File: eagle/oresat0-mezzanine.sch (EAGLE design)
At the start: 29 parts, among them J1 R107064070, J10 R107064070, J2 R107064070, J3 R107064070, J4 R107064070, J5 R107064070, J6 R107064070, J7 R107064070, J8 R107064070, J9 R107064070, U1 QBA-07+, U2 QBA-07+, U3 QBA-07+, U7 QCN-27+, U8 QCN-27+, U9 QCN-27+

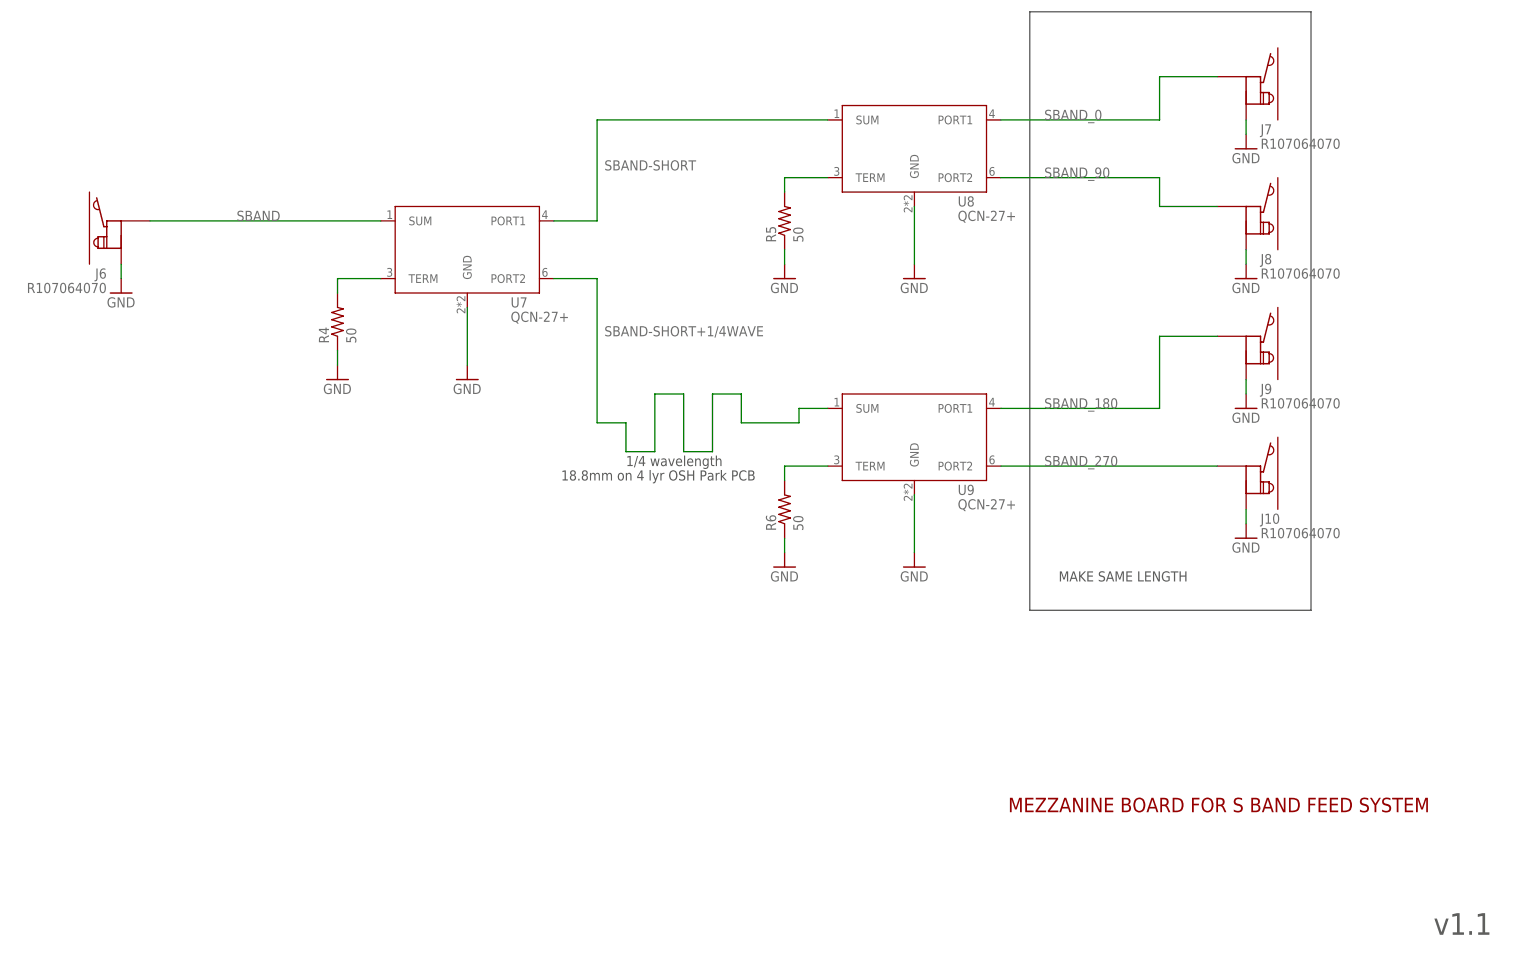
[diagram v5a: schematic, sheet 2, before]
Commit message: replaced S-band net labels with L1-band labels, swapped the S-band hybrids with L-band hybrids, recalculated 1/4 wavelength trace length, routed a new short+1/4 wavelength trace
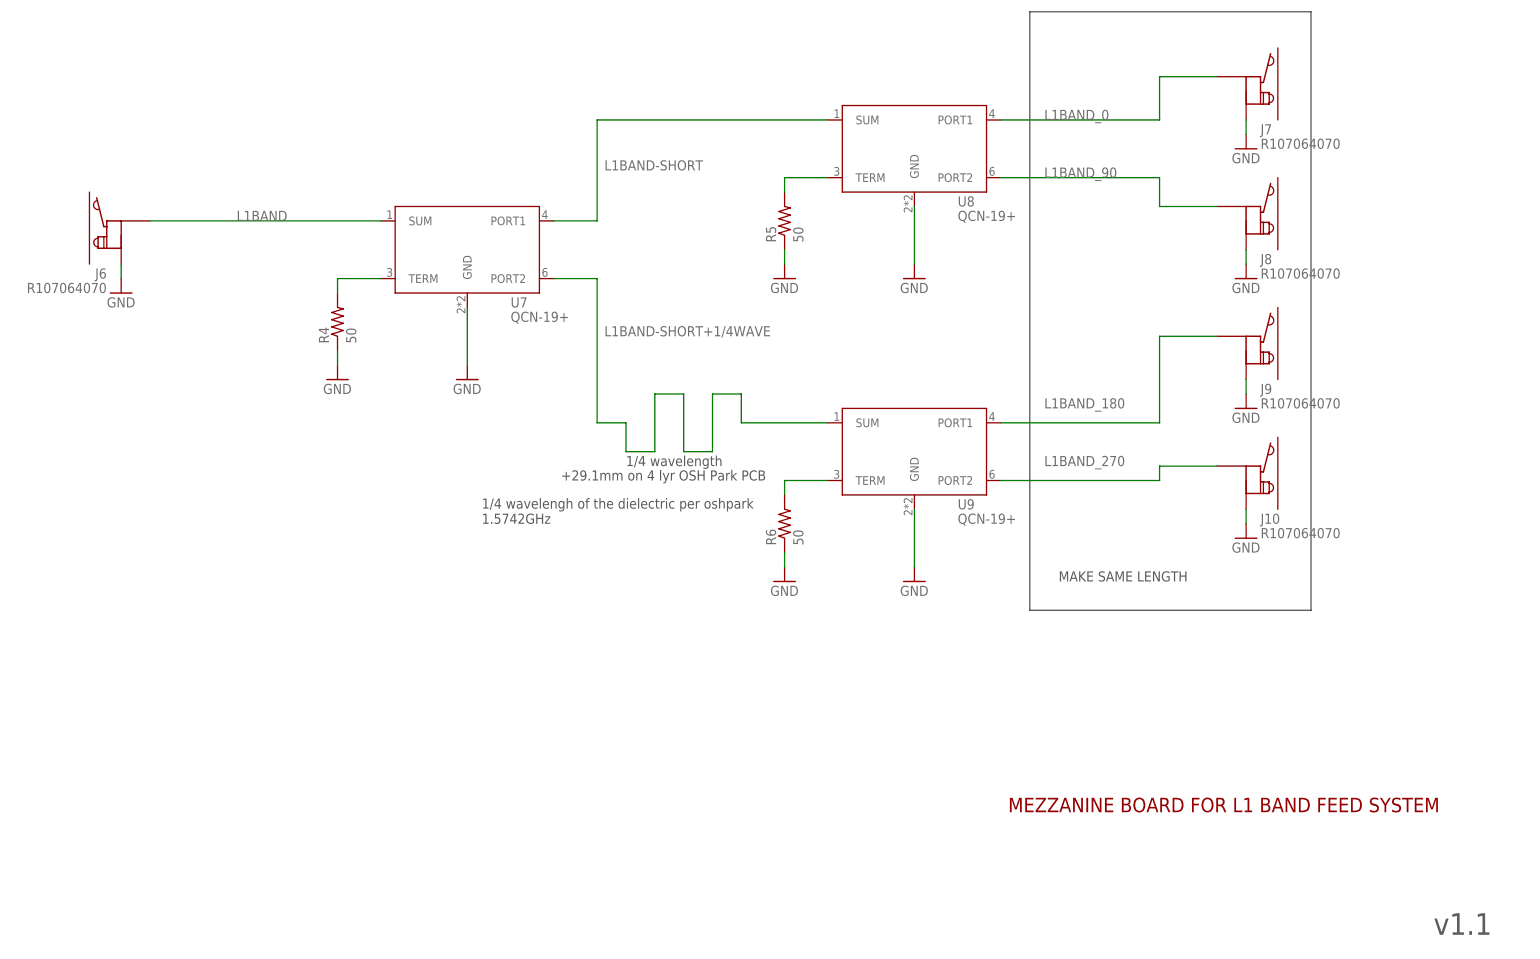
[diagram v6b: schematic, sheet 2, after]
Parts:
- U7, U8, U9: value QCN-27+ -> QCN-19+
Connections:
- net SBAND renamed L1BAND
- net SBAND-SHORT renamed L1BAND-SHORT
- net SBAND-SHORT+1/4WAVE renamed L1BAND-SHORT+1/4WAVE
- net SBAND_0 renamed L1BAND_0
- net SBAND_180 renamed L1BAND_180
- net SBAND_270 renamed L1BAND_270
- net SBAND_90 renamed L1BAND_90
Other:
- note added: "+29.1mm on 4 lyr OSH Park PCB"
- note added: "1/4 wavelengh of the dielectric per oshpark 1.5742GHz"
- note added: "MEZZANINE BOARD FOR L1 BAND FEED SYSTEM"
- note removed: "18.8mm on 4 lyr OSH Park PCB"
- note removed: "MEZZANINE BOARD FOR S BAND FEED SYSTEM"
- moved on the sheet: R6, U9
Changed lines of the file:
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@@
 <setting verticaltext="up"/>
 </settings>
-<grid distance="0.1" unitdist="inch" unit="inch" style="lines" multiple="1" display="no" altdistance="0.01" altunitdist="inch" altunit="inch"/>
+<grid distance="0.1" unitdist="inch" unit="inch" style="lines" multiple="1" display="yes" altdistance="0.01" altunitdist="inch" altunit="inch"/>
 <layers>
 <layer number="1" name="Top" color="4" fill="1" visible="no" active="no"/>
@@
 <part name="J9" library="J-Radiall-R107064070-RF" deviceset="R107064070" device=""/>
 <part name="J10" library="J-Radiall-R107064070-RF" deviceset="R107064070" device=""/>
-<part name="U7" library="U-MiniCirc-QCN-XXX+-quad" deviceset="QCN-XXX+" device="" value="QCN-27+"/>
-<part name="U8" library="U-MiniCirc-QCN-XXX+-quad" deviceset="QCN-XXX+" device="" value="QCN-27+"/>
-<part name="U9" library="U-MiniCirc-QCN-XXX+-quad" deviceset="QCN-XXX+" device="" value="QCN-27+"/>
+<part name="U7" library="U-MiniCirc-QCN-XXX+-quad" deviceset="QCN-XXX+" device="" value="QCN-19+"/>
+<part name="U8" library="U-MiniCirc-QCN-XXX+-quad" deviceset="QCN-XXX+" device="" value="QCN-19+"/>
+<part name="U9" library="U-MiniCirc-QCN-XXX+-quad" deviceset="QCN-XXX+" device="" value="QCN-19+"/>
 <part name="U$1" library="oresat-flight-marker" deviceset="FLIGHMARKER" device="NEW"/>
 <part name="FIDUCIAL2" library="monitor-v2-debug" deviceset="FIDUCIAL" device="-1.0X2.0"/>
@@
 <text x="-129.54" y="238.76" size="1.778" layer="97">1/4 wavelength</text>
 <text x="12.7" y="156.21" size="3.81" layer="97">v1.1</text>
-<text x="-62.23" y="177.8" size="2.54" layer="94">MEZZANINE BOARD FOR S BAND FEED SYSTEM</text>
-<text x="-140.97" y="236.22" size="1.778" layer="97">18.8mm on 4 lyr OSH Park PCB</text>
+<text x="-62.23" y="177.8" size="2.54" layer="94">MEZZANINE BOARD FOR L1 BAND FEED SYSTEM</text>
+<text x="-140.97" y="236.22" size="1.778" layer="97">+29.1mm on 4 lyr OSH Park PCB</text>
 <text x="-53.34" y="218.44" size="1.778" layer="97">MAKE SAME LENGTH</text>
 <wire x1="-58.42" y1="213.36" x2="-8.89" y2="213.36" width="0.1524" layer="97"/>
@@
 <wire x1="-8.89" y1="318.77" x2="-58.42" y2="318.77" width="0.1524" layer="97"/>
 <wire x1="-58.42" y1="318.77" x2="-58.42" y2="213.36" width="0.1524" layer="97"/>
+<text x="-154.94" y="228.6" size="1.778" layer="97">1/4 wavelengh of the dielectric per oshpark
+1.5742GHz</text>
 </plain>
 <instances>
@@
 <attribute name="VALUE" x="-81.28" y="269.24" size="1.778" layer="96"/>
 </instance>
-<instance part="GND13" gate="1" x="-78.74" y="220.98" smashed="yes">
-<attribute name="VALUE" x="-81.28" y="218.44" size="1.778" layer="96"/>
+<instance part="GND13" gate="1" x="-78.74" y="218.44" smashed="yes">
+<attribute name="VALUE" x="-81.28" y="215.9" size="1.778" layer="96"/>
 </instance>
 <instance part="GND15" gate="1" x="-180.34" y="254" smashed="yes">
@@
 <attribute name="VALUE" x="-104.14" y="269.24" size="1.778" layer="96"/>
 </instance>
-<instance part="GND17" gate="1" x="-101.6" y="220.98" smashed="yes">
-<attribute name="VALUE" x="-104.14" y="218.44" size="1.778" layer="96"/>
+<instance part="GND17" gate="1" x="-101.6" y="218.44" smashed="yes">
+<attribute name="VALUE" x="-104.14" y="215.9" size="1.778" layer="96"/>
 </instance>
 <instance part="GND18" gate="1" x="-218.44" y="269.24" smashed="yes">
@@
 <attribute name="VALUE" x="-98.298" y="278.13" size="1.778" layer="96" rot="R90"/>
 </instance>
-<instance part="R6" gate="R" x="-101.6" y="231.14" smashed="yes" rot="R90">
-<attribute name="NAME" x="-103.0986" y="227.33" size="1.778" layer="95" rot="R90"/>
-<attribute name="VALUE" x="-98.298" y="227.33" size="1.778" layer="96" rot="R90"/>
+<instance part="R6" gate="R" x="-101.6" y="228.6" smashed="yes" rot="R90">
+<attribute name="NAME" x="-103.0986" y="224.79" size="1.778" layer="95" rot="R90"/>
+<attribute name="VALUE" x="-98.298" y="224.79" size="1.778" layer="96" rot="R90"/>
 </instance>
 <instance part="J6" gate="G$1" x="-218.44" y="281.94" smashed="yes" rot="MR0">
@@
 <attribute name="VALUE" x="-71.12" y="281.94" size="1.778" layer="96"/>
 </instance>
-<instance part="U9" gate="G$1" x="-78.74" y="243.84" smashed="yes">
-<attribute name="NAME" x="-71.12" y="233.68" size="1.778" layer="95"/>
-<attribute name="VALUE" x="-71.12" y="231.14" size="1.778" layer="96"/>
+<instance part="U9" gate="G$1" x="-78.74" y="241.3" smashed="yes">
+<attribute name="NAME" x="-71.12" y="231.14" size="1.778" layer="95"/>
+<attribute name="VALUE" x="-71.12" y="228.6" size="1.778" layer="96"/>
 </instance>
 </instances>
@@
 <segment>
 <pinref part="GND17" gate="1" pin="GND"/>
-<wire x1="-101.6" y1="226.06" x2="-101.6" y2="223.52" width="0.1524" layer="91"/>
+<wire x1="-101.6" y1="223.52" x2="-101.6" y2="220.98" width="0.1524" layer="91"/>
 <pinref part="R6" gate="R" pin="1"/>
 </segment>
 <segment>
 <pinref part="GND13" gate="1" pin="GND"/>
-<wire x1="-78.74" y1="233.68" x2="-78.74" y2="223.52" width="0.1524" layer="91"/>
+<wire x1="-78.74" y1="231.14" x2="-78.74" y2="220.98" width="0.1524" layer="91"/>
 <pinref part="U9" gate="G$1" pin="GND"/>
 </segment>
@@
 <net name="N$5" class="0">
 <segment>
-<wire x1="-93.98" y1="238.76" x2="-101.6" y2="238.76" width="0.1524" layer="91"/>
-<wire x1="-101.6" y1="238.76" x2="-101.6" y2="236.22" width="0.1524" layer="91"/>
+<wire x1="-93.98" y1="236.22" x2="-101.6" y2="236.22" width="0.1524" layer="91"/>
+<wire x1="-101.6" y1="236.22" x2="-101.6" y2="233.68" width="0.1524" layer="91"/>
 <pinref part="R6" gate="R" pin="2"/>
 <pinref part="U9" gate="G$1" pin="TERM"/>
 </segment>
 </net>
-<net name="SBAND" class="1">
+<net name="L1BAND" class="1">
 <segment>
 <wire x1="-213.36" y1="281.94" x2="-172.72" y2="281.94" width="0.1524" layer="91"/>
@@
 </segment>
 </net>
-<net name="SBAND-SHORT" class="1">
+<net name="L1BAND-SHORT" class="1">
 <segment>
 <wire x1="-142.24" y1="281.94" x2="-134.62" y2="281.94" width="0.1524" layer="91"/>
@@
 </segment>
 </net>
-<net name="SBAND-SHORT+1/4WAVE" class="1">
-<segment>
-<wire x1="-99.06" y1="246.38" x2="-109.22" y2="246.38" width="0.1524" layer="91"/>
+<net name="L1BAND-SHORT+1/4WAVE" class="1">
+<segment>
 <wire x1="-109.22" y1="246.38" x2="-109.22" y2="251.46" width="0.1524" layer="91"/>
 <wire x1="-109.22" y1="251.46" x2="-114.3" y2="251.46" width="0.1524" layer="91"/>
@@
 <pinref part="U7" gate="G$1" pin="PORT2"/>
 <pinref part="U9" gate="G$1" pin="SUM"/>
-<wire x1="-93.98" y1="248.92" x2="-99.06" y2="248.92" width="0.1524" layer="91"/>
-<wire x1="-99.06" y1="248.92" x2="-99.06" y2="246.38" width="0.1524" layer="91"/>
-</segment>
-</net>
-<net name="SBAND_0" class="1">
+<wire x1="-93.98" y1="246.38" x2="-109.22" y2="246.38" width="0.1524" layer="91"/>
+</segment>
+</net>
+<net name="L1BAND_0" class="1">
 <segment>
 <wire x1="-35.56" y1="299.72" x2="-35.56" y2="307.34" width="0.1524" layer="91"/>
@@
 </segment>
 </net>
-<net name="SBAND_90" class="1">
+<net name="L1BAND_90" class="1">
 <segment>
 <label x="-55.88" y="289.56" size="1.778" layer="95"/>
@@
 </segment>
 </net>
-<net name="SBAND_180" class="1">
-<segment>
-<wire x1="-63.5" y1="248.92" x2="-35.56" y2="248.92" width="0.1524" layer="91"/>
+<net name="L1BAND_180" class="1">
+<segment>
 <label x="-55.88" y="248.92" size="1.778" layer="95"/>
-<wire x1="-35.56" y1="248.92" x2="-35.56" y2="261.62" width="0.1524" layer="91"/>
+<wire x1="-35.56" y1="246.38" x2="-35.56" y2="261.62" width="0.1524" layer="91"/>
 <wire x1="-35.56" y1="261.62" x2="-25.4" y2="261.62" width="0.1524" layer="91"/>
 <pinref part="J9" gate="G$1" pin="P$1"/>
 <pinref part="U9" gate="G$1" pin="PORT1"/>
-</segment>
-</net>
-<net name="SBAND_270" class="1">
+<wire x1="-35.56" y1="246.38" x2="-63.5" y2="246.38" width="0.1524" layer="91"/>
+</segment>
+</net>
+<net name="L1BAND_270" class="1">
 <segment>
 <label x="-55.88" y="238.76" size="1.778" layer="95"/>
 <pinref part="J10" gate="G$1" pin="P$1"/>
 <pinref part="U9" gate="G$1" pin="PORT2"/>
-<wire x1="-63.5" y1="238.76" x2="-25.4" y2="238.76" width="0.1524" layer="91"/>
+<wire x1="-63.5" y1="236.22" x2="-35.56" y2="236.22" width="0.1524" layer="91"/>
+<wire x1="-35.56" y1="236.22" x2="-35.56" y2="238.76" width="0.1524" layer="91"/>
+<wire x1="-35.56" y1="238.76" x2="-25.4" y2="238.76" width="0.1524" layer="91"/>
 </segment>
 </net>
@@
 </drawing>
 <compatibility>
+<note version="6.3" minversion="6.2.2" severity="warning">
+Since Version 6.2.2 text objects can contain more than one line,
+which will not be processed correctly with this version.
+</note>
 <note version="8.2" severity="warning">
 Since Version 8.2, EAGLE supports online libraries. The ids

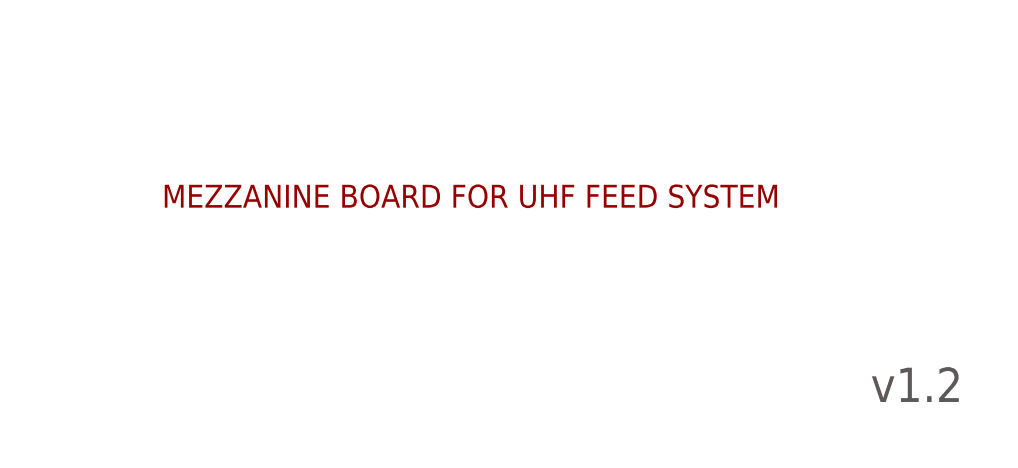
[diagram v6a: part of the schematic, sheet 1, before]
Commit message: v2.0 card, mezzanine, and BOM for v2.0. Moved UHF hybrids to avoid melt wire resistor leads. Updated BOM to reflect new v2.0 design.
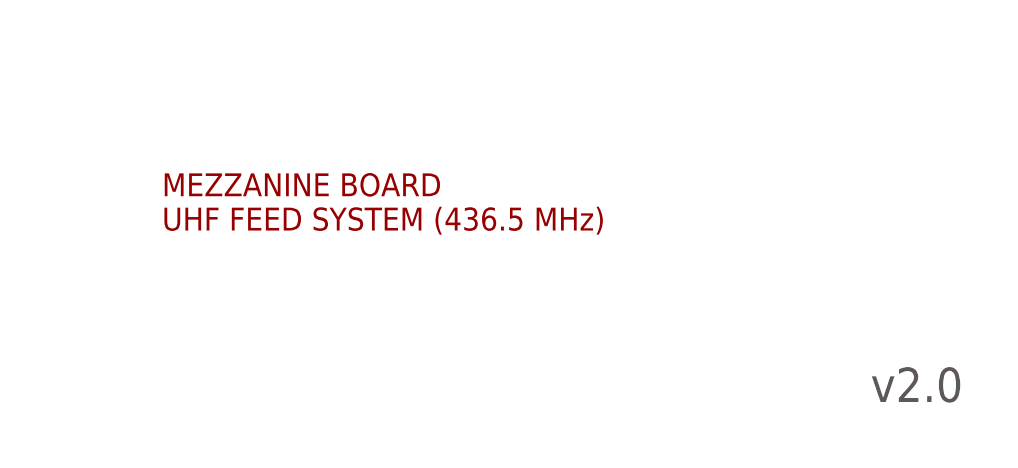
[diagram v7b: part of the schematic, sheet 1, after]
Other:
- note added: "L1 BAND FEED SYSTEM (1.575 GHz)"
- note added: "MEZZANINE BOARD UHF FEED SYSTEM (436.5 MHz)"
- note added: "v2.0"
- note removed: "MEZZANINE BOARD FOR L1 BAND FEED SYSTEM"
- note removed: "MEZZANINE BOARD FOR UHF FEED SYSTEM"
- note removed: "v1.2"
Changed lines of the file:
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@@
 <setting verticaltext="up"/>
 </settings>
-<grid distance="0.1" unitdist="inch" unit="inch" style="lines" multiple="1" display="yes" altdistance="0.01" altunitdist="inch" altunit="inch"/>
+<grid distance="0.1" unitdist="inch" unit="inch" style="lines" multiple="1" display="no" altdistance="0.01" altunitdist="inch" altunit="inch"/>
 <layers>
 <layer number="1" name="Top" color="4" fill="1" visible="no" active="no"/>
@@
 <plain>
 <text x="119.38" y="88.9" size="1.778" layer="97">1/4 wavelength</text>
-<text x="261.62" y="6.35" size="3.81" layer="97">v1.2</text>
-<text x="182.88" y="27.94" size="2.54" layer="94">MEZZANINE BOARD FOR UHF FEED SYSTEM</text>
+<text x="261.62" y="6.35" size="3.81" layer="97">v2.0</text>
+<text x="182.88" y="25.4" size="2.54" layer="94">MEZZANINE BOARD
+UHF FEED SYSTEM (436.5 MHz)</text>
 <text x="200.66" y="66.04" size="1.778" layer="97">MAKE SAME LENGTH</text>
 <wire x1="187.96" y1="60.96" x2="245.11" y2="60.96" width="0.1524" layer="97"/>
@@
 </sheet>
 <sheet>
-<description>S BAND</description>
+<description>L1 BAND</description>
 <plain>
 <text x="-129.54" y="238.76" size="1.778" layer="97">1/4 wavelength</text>
 <text x="12.7" y="156.21" size="3.81" layer="97">v1.1</text>
-<text x="-62.23" y="177.8" size="2.54" layer="94">MEZZANINE BOARD FOR L1 BAND FEED SYSTEM</text>
+<text x="-57.15" y="177.8" size="2.54" layer="94">L1 BAND FEED SYSTEM (1.575 GHz)</text>
 <text x="-140.97" y="236.22" size="1.778" layer="97">+29.1mm on 4 lyr OSH Park PCB</text>
 <text x="-53.34" y="218.44" size="1.778" layer="97">MAKE SAME LENGTH</text>
